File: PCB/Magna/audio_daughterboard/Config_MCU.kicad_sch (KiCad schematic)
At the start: 1 part, among them U1306 STM32F030C8Tx

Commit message: Some updates to PCB
Honestly I cannot remember whats changed
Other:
- moved on the sheet: U1306

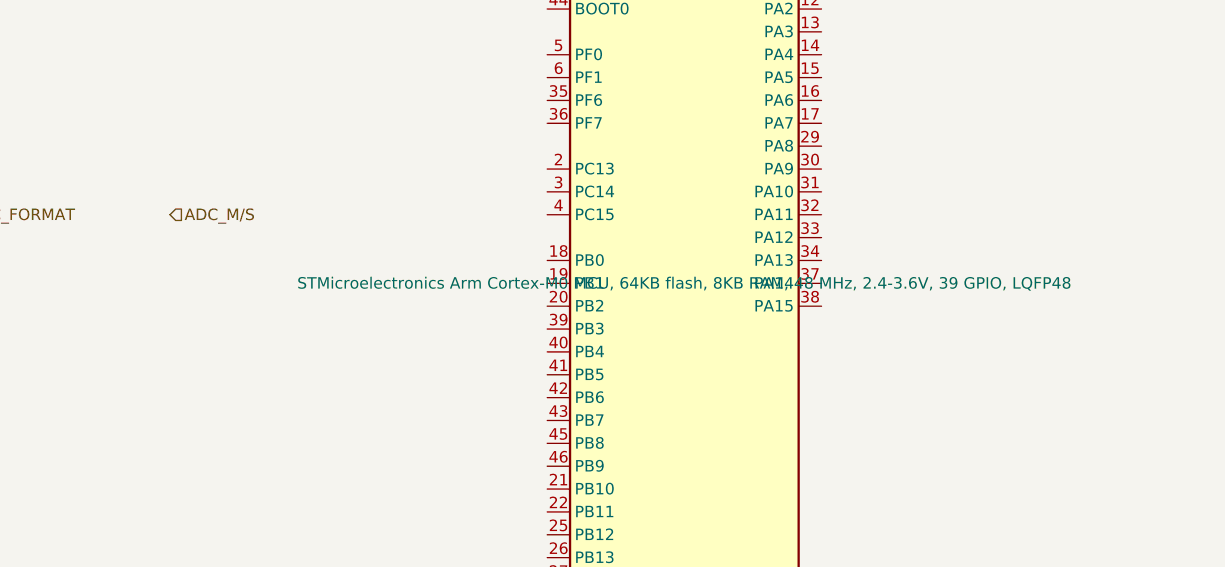
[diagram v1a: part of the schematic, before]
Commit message: Update schematics to Kicad 9
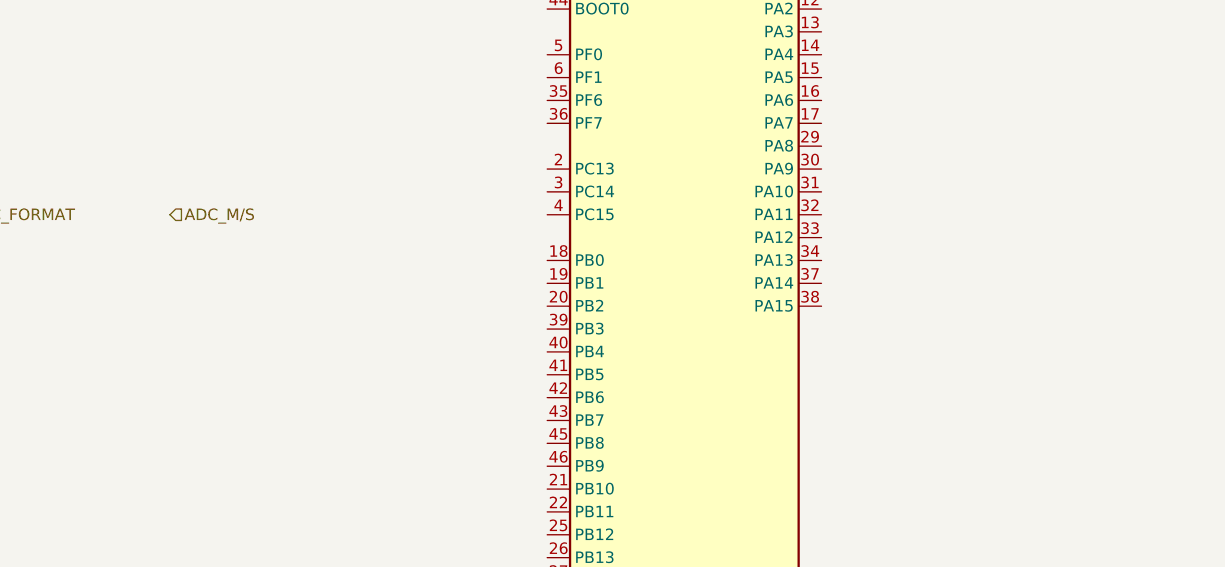
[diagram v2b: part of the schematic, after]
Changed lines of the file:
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@@
 					(size 1.27 1.27)
 				)
+				(hide yes)
 			)
 		)

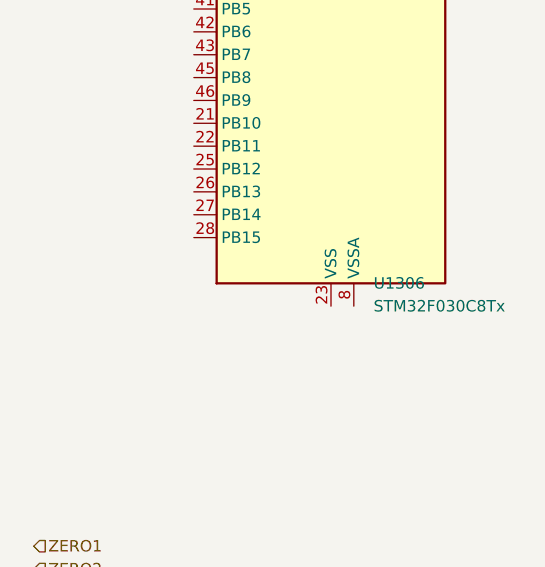
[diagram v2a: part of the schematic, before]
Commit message: Update audio PCB
Mainly added simulations to Linedriver and DAC.

Also fixed some small issues that was found when simulating
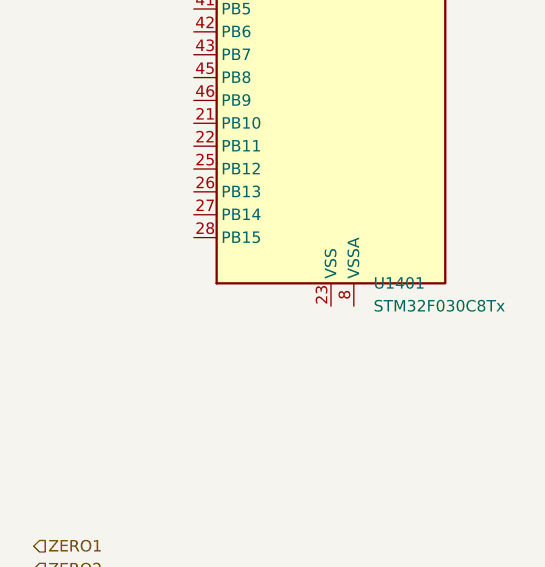
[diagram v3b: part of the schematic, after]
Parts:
- renumbered U1306 to U1401
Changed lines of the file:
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@@
 		(at 106.68 95.25 0)
 		(unit 1)
-		(exclude_from_sim no)
+		(exclude_from_sim yes)
 		(in_bom yes)
 		(on_board yes)
 		(dnp no)
 		(fields_autoplaced yes)
-		(property "Reference" "U1306"
+		(property "Reference" "U1401"
 			(at 111.4141 135.89 0)
 			(effects
@@
 			(project "Audio_daughterboard"
 				(path "/1eadd930-2484-4c28-b568-78e6454e7f52/cb6edb6e-4478-4049-8c56-b1719d2a2d5b"
-					(reference "U1306")
+					(reference "U1401")
 					(unit 1)
 				)

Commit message: "Finalize" Audio daugherboard
Finished DAC output filter
Fixed the whole damn MCU subschematic
Fixed Linedriver schematic
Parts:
- added C1401: 100nF, Capacitor_SMD:C_0805_2012Metric_Pad1.18x1.45mm_HandSolder, symbol Device:C
- added C1402, C1403, C1404, C1405: 4.7uF, Capacitor_SMD:C_0805_2012Metric_Pad1.18x1.45mm_HandSolder, symbol Device:C
- added J1401: Conn_01x03_Pin, symbol Connector:Conn_01x03_Pin
- added J1402: Conn_ARM_SWD_TagConnect_TC2030, Connector:Tag-Connect_TC2030-IDC-FP_2x03_P1.27mm_Vertical, symbol Connector:Conn_ARM_SWD_TagConnect_TC2030
- added J1403, J1404: Conn_01x02_Pin, symbol Connector:Conn_01x02_Pin
- added R1401: 10k, Resistor_SMD:R_0805_2012Metric_Pad1.20x1.40mm_HandSolder, symbol Device:R
- U1401: symbol MCU_ST_STM32F0:STM32F030C8Tx -> MCU_ST_STM32F0:STM32F030C6Tx
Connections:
- net ADC_FORMAT: now also U1401.25 (PB12)
- net ADC_FSAMPEN: now also U1401.27 (PB14)
- net ADC_IWL: now also U1401.22 (PB11)
- net ADC_M/S: now also U1401.26 (PB13)
- net AMP_CLK: now also U1401.29 (PA8)
- net AMP_DATA: now also U1401.30 (PA9)
- net AMP_LOAD_0: now also U1401.28 (PB15)
- net AMP_LOAD_1: now also U1401.32 (PA11)
- net CFG_SPI_CLK: now also U1401.15 (PA5)
- net CFG_SPI_MISO: now also U1401.16 (PA6)
- net CFG_SPI_MOSI: now also U1401.17 (PA7)
- net CFG_SPI_NCS: now also U1401.14 (PA4)
- net DAC_MUTE: now also U1401.46 (PB9)
- net DAC_RST: now also U1401.39 (PB3)
- net MC/SCL/DMT: now also U1401.42 (PB6)
- net MD/SDA/DEMP: now also U1401.43 (PB7)
- net MODE: now also U1401.45 (PB8)
- net SEL_DAC0: now also U1401.40 (PB4)
- net SEL_DAC1: now also U1401.41 (PB5)
- net VDD: now reaches U1401.1 (VDD)
- net VDD: now also U1401.24 (VDD), U1401.48 (VDD), U1401.9 (VDDA), C1402.1, C1403.1, C1404.1, C1405.1, J1402.1 (VCC), J1403.1 (Pin_1)
- net VAA_ENABLE: now reaches U1401.20 (PB2)
- net GND: now reaches U1401.23 (VSS), U1401.47 (VSS)
- net GND: now also U1401.8 (VSSA), C1401.2, C1402.2, C1403.2, C1404.2, C1405.2, J1401.3 (Pin_3), J1402.5 (GND), J1404.2 (Pin_2), R1401.2
- net USART_RX: now reaches U1401.31 (PA10)
- net SWDIO: now reaches U1401.34 (PA13)
- net SWDIO: now also J1401.2 (Pin_2), J1402.2 (SWDIO)
- net DAC1_ZERO2: now reaches U1401.35 (PF6)
- net DAC1_ZERO1: now reaches U1401.36 (PF7)
- net SWCLK: now reaches U1401.37 (PA14)
- net SWCLK: now also J1401.1 (Pin_1), J1402.4 (SWCLK)
- net MCU_BOOT0: now reaches U1401.44 (BOOT0)
- net MCU_BOOT0: now also J1403.2 (Pin_2), R1401.1
- net DAC0_ZERO2: now reaches U1401.5 (PF0)
- net DAC0_ZERO1: now reaches U1401.6 (PF1)
- net MCU_NRST: now reaches U1401.7 (NRST)
- net MCU_NRST: now also C1401.1, J1402.3 (~{RESET}), J1404.1 (Pin_1)
- no-connect marks 0 -> 14
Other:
- note added: "Decoupling caps are a bit big, but since the same size is used anyways I see no reason to use another value"
